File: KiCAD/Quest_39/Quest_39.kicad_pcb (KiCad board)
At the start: 4 copper layers, 398 parts, among them J1 1x2 Scr. Term., J10 1x2 Scr. Term., J11 1x2 Scr. Term., J12 Conn_01x05_Male, J2 1x2 Scr. Term., J3 1x2 Scr. Term., J4 1x2 Scr. Term., J5 1x2 Scr. Term., J6 1x2 Scr. Term., J7 1x2 Scr. Term., J8 1x2 Scr. Term., J9 1x2 Scr. Term., U1 AZ1117-3.3, U10 LTM4611EV-PBF, U11 MCP4151-502E/SN, U12 AD626ANZ, U13 INA226, U14 LTM4611EV-PBF, U15 MCP4151-502E/SN, U16 AD626ANZ, U17 INA226, U18 LTM4611EV-PBF, U19 MCP4151-502E/SN, U2 17791063215, U20 AD626ANZ, U21 INA226, U22 LTM4611EV-PBF, U23 MCP4151-502E/SN, U24 AD626ANZ, U25 INA226, U26 LTM4611EV-PBF, U27 MCP4151-502E/SN, U28 AD626ANZ, U29 INA226, U3 STM32F103C8T6, U30 LTM4611EV-PBF, U31 MCP4151-502E/SN, U32 AD626ANZ, U33 INA226, U34 LTM4611EV-PBF, U35 MCP4151-502E/SN, U36 AD626ANZ, U37 INA226, U38 LTM4611EV-PBF, U39 MCP4151-502E/SN, U4 AD626ANZ, U40 AD626ANZ, U41 INA226, U42 LTM4611EV-PBF, U43 MCP4151-502E/SN, U5 INA226, U6 LTM4611EV-PBF, U7 MCP4151-502E/SN, U8 AD626ANZ, U9 INA226, Y1 16MHz

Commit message: Finished routing I2C, SPI and all 10 CS
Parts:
- added TP76: TestPoint, TestPoint:TestPoint_Pad_D2.0mm, F.Cu at (134.1, 77.9)
- added TP77: TestPoint, TestPoint:TestPoint_Pad_D2.0mm, F.Cu at (162.4, 89.3)
- moved R3 151.3 mm to (149.7, 74.4), turned to -90 degrees
- moved H5 143.7 mm to (155.6, 123.6)
- moved TP1 130.7 mm to (145.8, 70.4), turned to 180 degrees
- moved R11 125.3 mm to (146.8, 100.4), turned to -90 degrees
- moved TP5 119.6 mm to (127.8, 73.7), turned to 180 degrees
- moved R15 119.2 mm to (157.8, 100.4), turned to -90 degrees
- moved R13 113.7 mm to (152.3, 100.4), turned to -90 degrees
- moved R8 111.0 mm to (138.6, 100.4), turned to -90 degrees
- moved R12 110.4 mm to (149.5, 100.4), turned to -90 degrees
- moved R14 104.8 mm to (155.0, 100.4), turned to -90 degrees
- moved C1 104.6 mm to (144.2, 76.1), turned to 0 degrees
- moved R10 102.8 mm to (144.1, 100.4), turned to -90 degrees
- moved TP4 101.7 mm to (168.0, 89.4), turned to 180 degrees
- moved R7 97.7 mm to (135.8, 100.4), turned to -90 degrees
- moved R16 94.7 mm to (160.5, 100.4), turned to -90 degrees
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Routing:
- net /SCL: track 6.81 -> 877.1 mm, vias 0 -> 16
- net /SDA: track 11.8 -> 868.1 mm, vias 0 -> 10
- net /SCK: track 0.00 -> 456.7 mm, vias 0 -> 16
- net /SDIO: track 0.00 -> 452.6 mm, vias 0 -> 13
- net /CS4: track 0.00 -> 158.3 mm, vias 0 -> 4
- net /CS5: track 0.00 -> 143.2 mm, vias 0 -> 4
- net /CS3: track 0.00 -> 117.8 mm, vias 0 -> 4
- net /CS9: track 0.00 -> 106.1 mm, vias 0 -> 6
- net /CS6: track 0.00 -> 100.3 mm, vias 0 -> 6
- net /CS0: track 0.00 -> 90.8 mm, vias 0 -> 4
- net /CS2: track 0.00 -> 80.4 mm, vias 0 -> 4
- net /CS8: track 0.00 -> 62.0 mm, vias 0 -> 6
- net +3.3V: track 76.1 -> 136.7 mm, vias 3 -> 4
- net /CS1: track 0.00 -> 55.7 mm, vias 0 -> 4
- net /CS7: track 0.00 -> 54.2 mm, vias 0 -> 6
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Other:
- board text removed: "To do: - 3V3 regulator met componenten plaatsen - 5V converter plaatsen - mounting hole in het midden - SDA, SCL - SCK, SDIO - SC met pull-up"

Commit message: Top layer power planes added
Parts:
- moved TP41 2.78 mm to (187.4, 229.3)
- moved H1 1.49 mm to (54.3, 257.0)
- moved R43 1.16 mm to (110.0, 206.4)
- moved C68 0.86 mm to (98.2, 219.2)
- moved C70 0.86 mm to (93.3, 219.2)
- moved C71 0.86 mm to (90.8, 219.2)
- moved C69 0.86 mm to (95.7, 219.2)
- moved C161 0.81 mm to (201.0, 41.8)
- moved C158 0.81 mm to (193.9, 41.8)
- moved C159 0.81 mm to (196.2, 41.8)
- moved C160 0.81 mm to (198.6, 41.8)
- moved C128 0.81 mm to (193.6, 129.6)
- moved C129 0.81 mm to (196.0, 129.6)
- moved C130 0.81 mm to (198.5, 129.6)
- moved C131 0.81 mm to (200.9, 129.6)
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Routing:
- net /SDA: track 868.1 -> 960.0 mm, vias 10 -> 12
- net /SCL: track 877.1 -> 968.3 mm, vias 16 -> 18
- net /BUCK_4/BUCK_VIN: track 5.23 -> 8.51 mm
- net Net-(TP27-Pad1): track 6.37 -> 4.41 mm
- net /NEG_1: track 32.1 -> 30.5 mm
- net /NEG_0: track 26.2 -> 24.8 mm
- net /NEG_2: track 30.9 -> 29.6 mm
- net GND: track 124.8 -> 126.1 mm, vias 69 -> 70
- net /NEG_4: track 31.8 -> 30.7 mm
- net Net-(TP41-Pad1): track 4.75 -> 5.53 mm
- added copper zone on F.Cu, net /POS_9

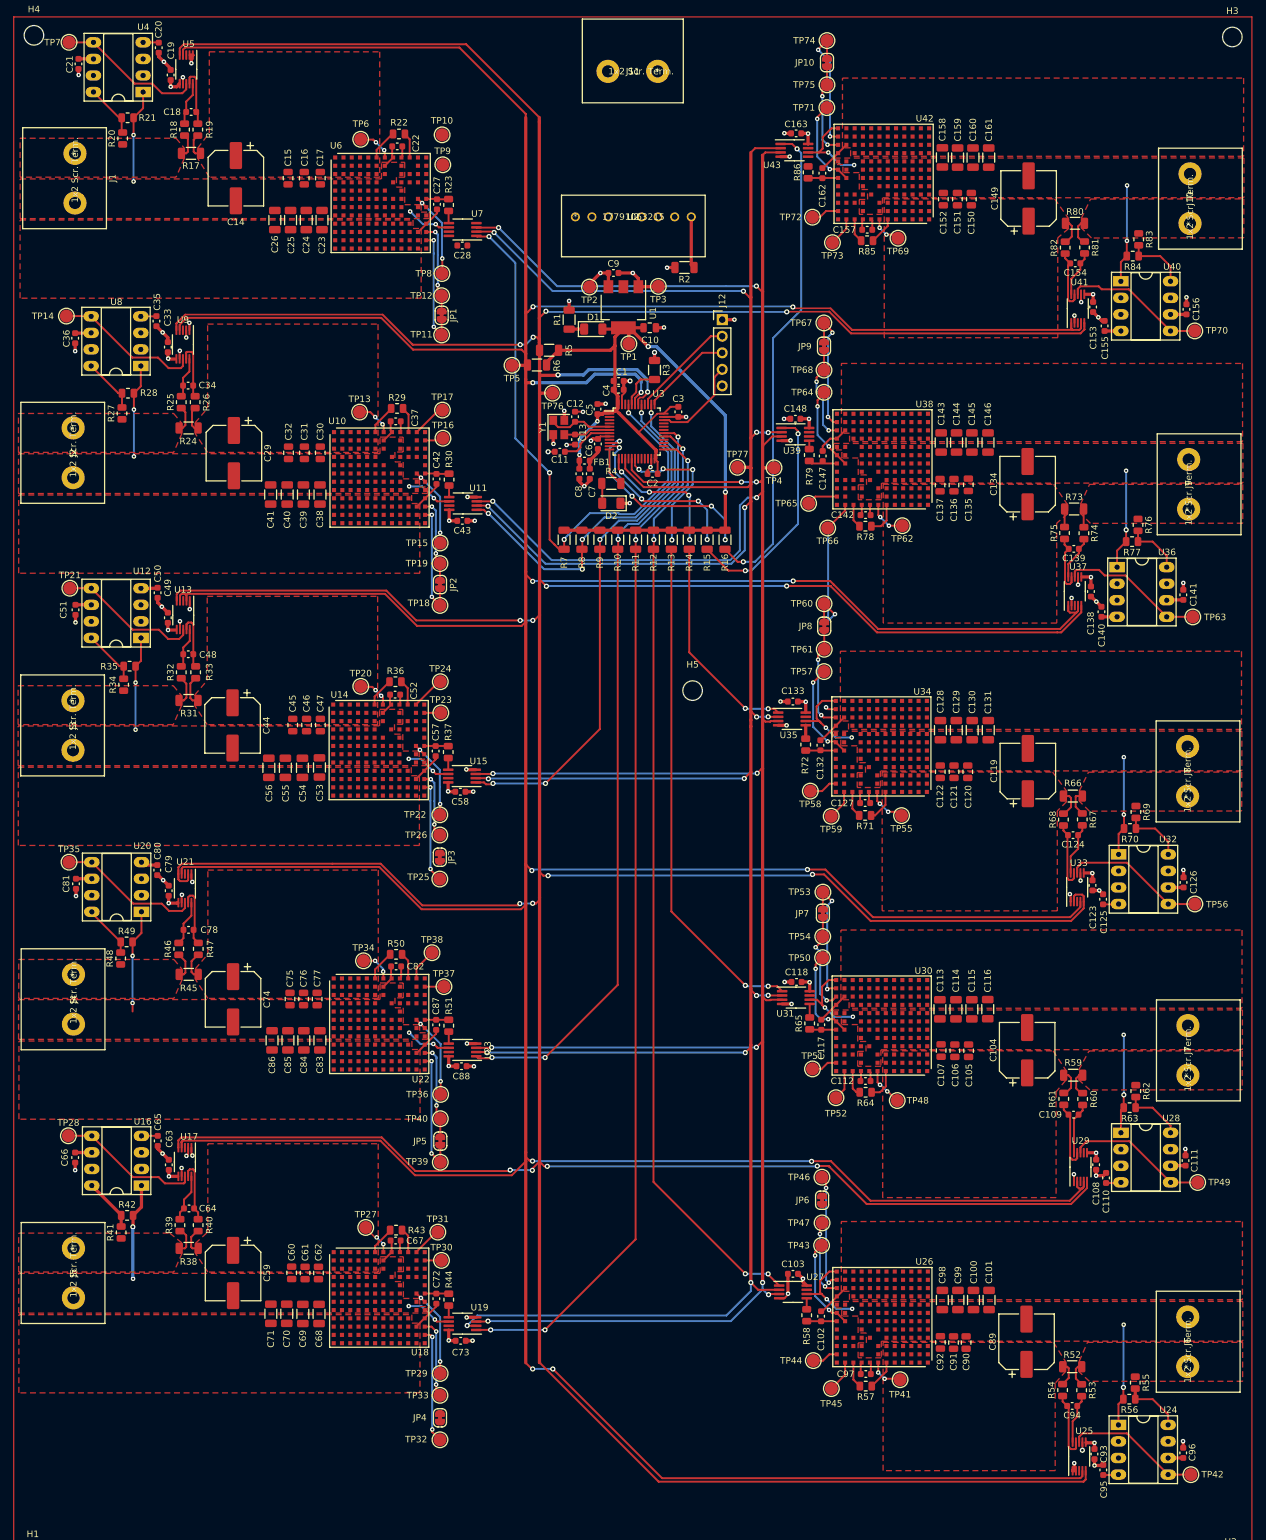
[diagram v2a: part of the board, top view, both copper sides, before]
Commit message: Executed DRC and fixed issues. Started work on bottom power planes
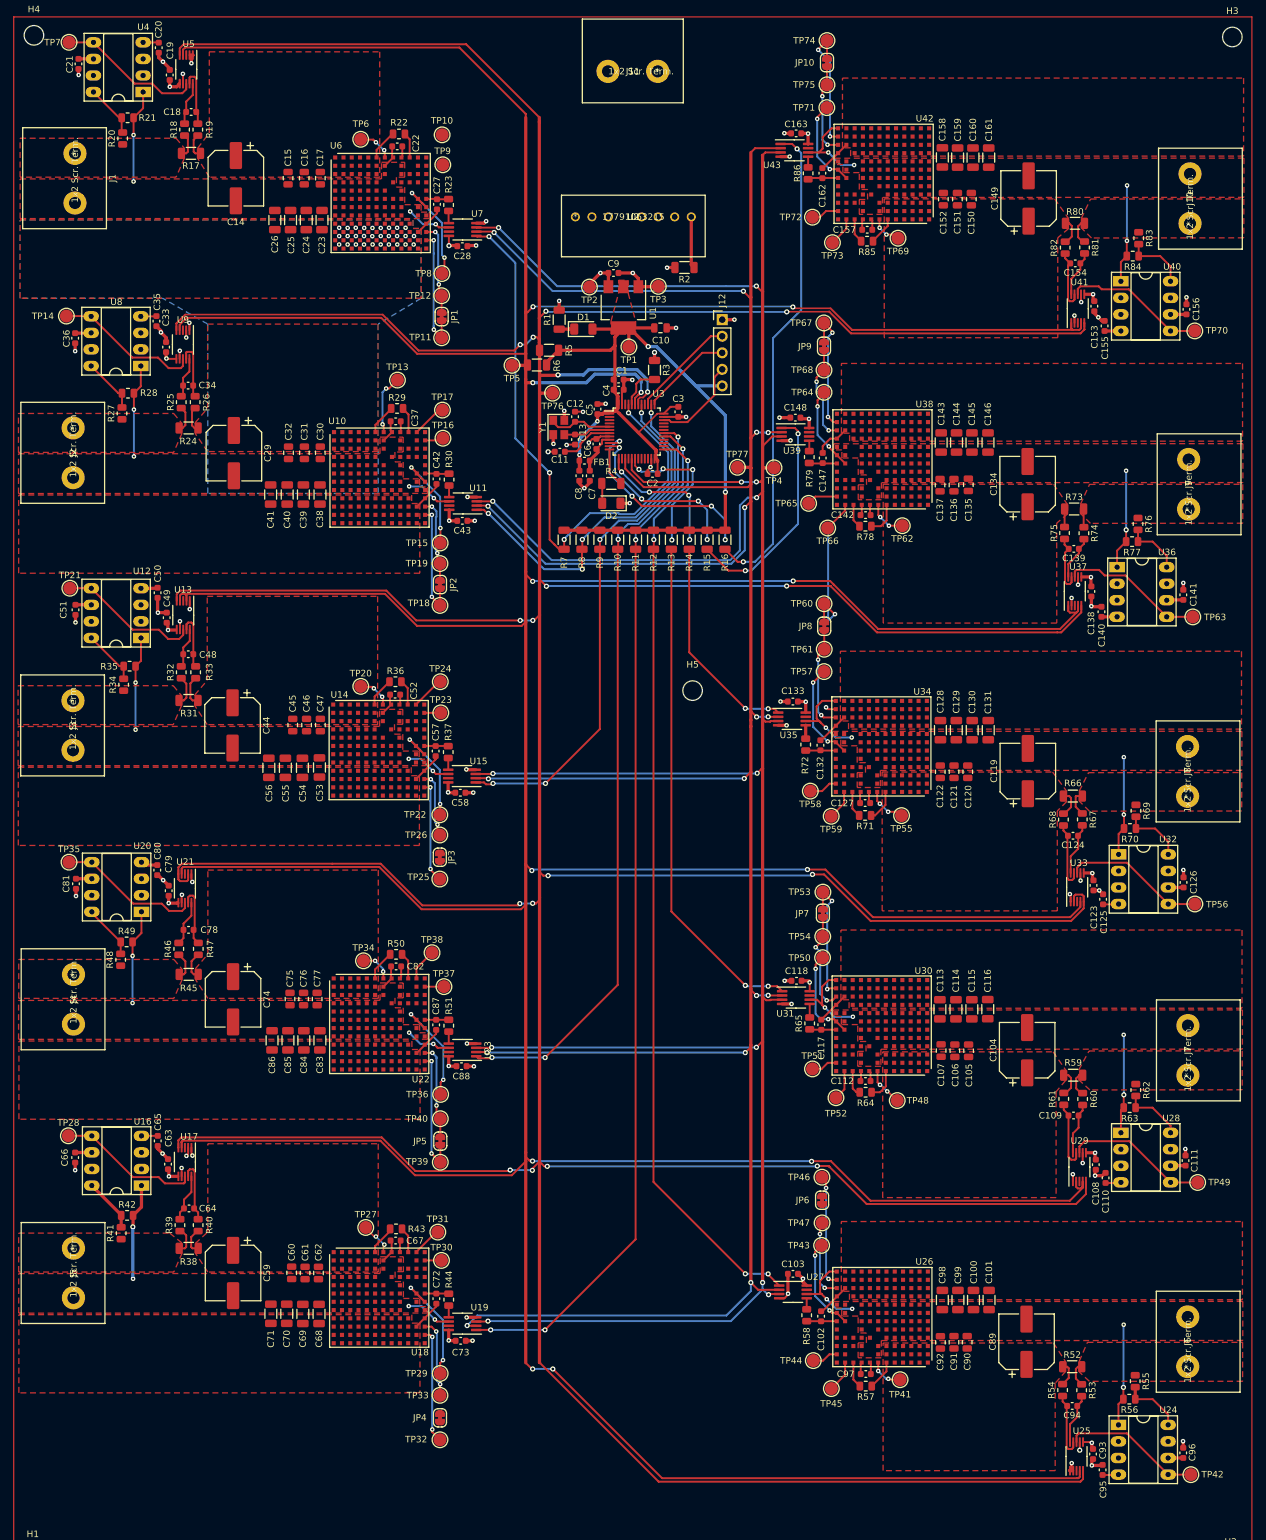
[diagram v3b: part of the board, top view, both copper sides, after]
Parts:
- moved TP13 7.60 mm to (110.3, 75.9)
- moved C10 1.65 mm to (150.6, 67.9)
- moved D1 1.52 mm to (138.8, 68.1)
- moved R1 1.52 mm to (135.1, 66.6)
- moved TP1 0.48 mm to (145.8, 70.8)
- moved TP11 0.43 mm to (117.0, 69.4)
- moved U25 0.40 mm to (214.5, 241.1)
- moved C147 0.31 mm to (175.5, 87.9)
- moved R79 0.31 mm to (173.5, 87.7)
- moved C7 0.31 mm to (139.8, 90.6)
- moved C8 0.31 mm to (138.2, 90.6)
- moved C33 0.27 mm to (74.8, 70.9)
- moved C153 0.23 mm to (217.2, 64.6)
- moved C93 0.23 mm to (217.0, 240.7)
- moved C6 0.23 mm to (140.8, 85.7)
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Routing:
- net +3.3V: track 136.7 -> 146.3 mm
- net GND: track 126.1 -> 133.7 mm, vias 70 -> 73
- net Net-(TP15-Pad1): track 11.5 -> 16.6 mm
- net Net-(TP29-Pad1): track 14.6 -> 18.4 mm
- net Net-(TP13-Pad1): track 5.50 -> 9.26 mm
- net Net-(TP36-Pad1): track 13.9 -> 17.5 mm
- net Net-(TP22-Pad1): track 13.1 -> 16.7 mm
- net +5V: track 87.5 -> 90.6 mm, vias 26 -> 27
- net +3.3VA: track 3.63 -> 6.53 mm
- net Net-(TP8-Pad1): track 14.8 -> 17.7 mm
- net /SCL: track 968.3 -> 970.0 mm
- net /BUCK_9/P0A: track 0.00 -> 1.64 mm
- net /NEG_3: track 31.3 -> 30.0 mm
- net Net-(JP6-Pad2): track 18.0 -> 17.4 mm
- net /SDA: track 960.0 -> 960.7 mm
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- added copper zone on F.Cu, net +3.3V
- added copper zone on B.Cu, net /NEG_1
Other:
- board text added: "{ "ViaStitching": "0.1", "stitch_zone_0": { "HSpacing": "1.27", "VSpacing": "1.27", "Clearance": "0.2", "Randomize": false } }"
